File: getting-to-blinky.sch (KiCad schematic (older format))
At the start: 7 parts

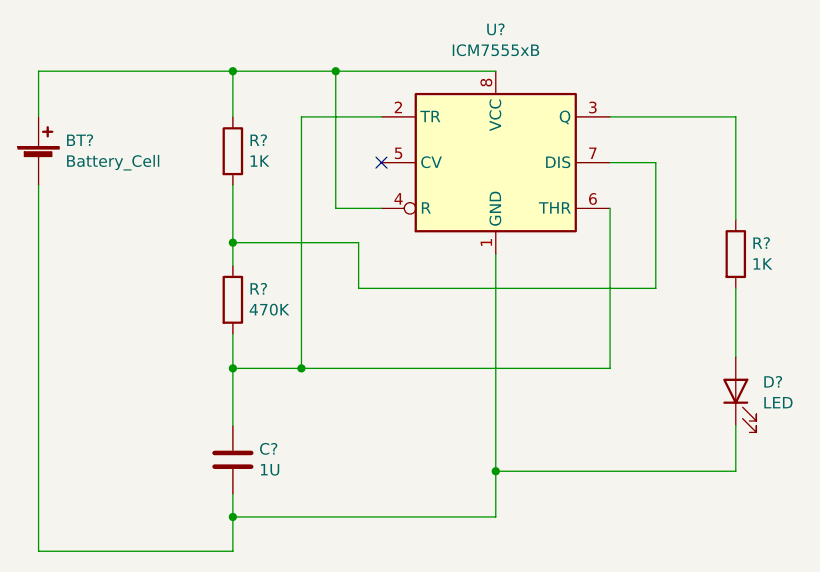
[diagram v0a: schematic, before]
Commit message: Annotate and assign footprints.
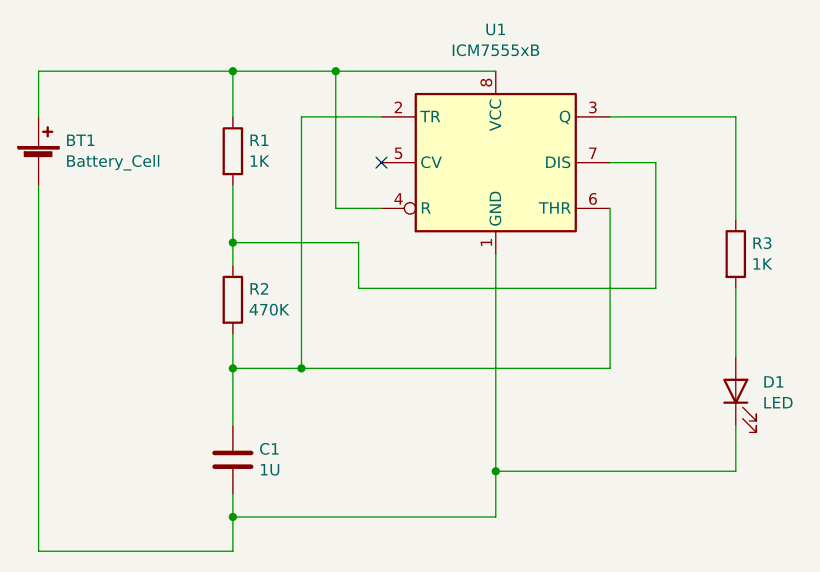
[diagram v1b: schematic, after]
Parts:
- BT1: renamed from BT?; footprint (none) -> electronics-getting-to-blinky:S8211-46R
- D1: renamed from D?; footprint (none) -> LED_SMD:LED_0805_2012Metric_Pad1.15x1.40mm_HandSolder
- gave numbers to parts that had none: 5
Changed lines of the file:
@@
 $EndDescr
 $Comp
-L Timer:ICM7555xB U?
+L Timer:ICM7555xB U1
 U 1 1 5F0270B9
 P 5550 4000
-F 0 "U?" H 5550 4581 50  0000 C CNN
+F 0 "U1" H 5550 4581 50  0000 C CNN
 F 1 "ICM7555xB" H 5550 4490 50  0000 C CNN
 F 2 "Package_SO:SOIC-8_3.9x4.9mm_P1.27mm" H 6400 3600 50  0001 C CNN
@@
 $EndComp
 $Comp
-L Device:R R?
+L Device:R R1
 U 1 1 5F0303EF
 P 4400 3950
-F 0 "R?" H 4470 3996 50  0000 L CNN
+F 0 "R1" H 4470 3996 50  0000 L CNN
 F 1 "1K" H 4470 3905 50  0000 L CNN
 F 2 "Resistor_SMD:R_0805_2012Metric_Pad1.15x1.40mm_HandSolder" V 4330 3950 50  0001 C CNN
@@
 $EndComp
 $Comp
-L Device:R R?
+L Device:R R2
 U 1 1 5F031116
 P 4400 4600
-F 0 "R?" H 4470 4646 50  0000 L CNN
+F 0 "R2" H 4470 4646 50  0000 L CNN
 F 1 "470K" H 4470 4555 50  0000 L CNN
 F 2 "Resistor_SMD:R_0805_2012Metric_Pad1.15x1.40mm_HandSolder" V 4330 4600 50  0001 C CNN
@@
 $EndComp
 $Comp
-L Device:R R?
+L Device:R R3
 U 1 1 5F031486
 P 6600 4400
-F 0 "R?" H 6670 4446 50  0000 L CNN
+F 0 "R3" H 6670 4446 50  0000 L CNN
 F 1 "1K" H 6670 4355 50  0000 L CNN
 F 2 "Resistor_SMD:R_0805_2012Metric_Pad1.15x1.40mm_HandSolder" V 6530 4400 50  0001 C CNN
@@
 $EndComp
 $Comp
-L Device:C C?
+L Device:C C1
 U 1 1 5F031D64
 P 4400 5300
-F 0 "C?" H 4515 5346 50  0000 L CNN
+F 0 "C1" H 4515 5346 50  0000 L CNN
 F 1 "1U" H 4515 5255 50  0000 L CNN
 F 2 "Capacitor_SMD:C_0805_2012Metric_Pad1.15x1.40mm_HandSolder" H 4438 5150 50  0001 C CNN
@@
 $EndComp
 $Comp
-L Device:Battery_Cell BT?
+L Device:Battery_Cell BT1
 U 1 1 5F03267C
 P 3550 4000
-F 0 "BT?" H 3668 4096 50  0000 L CNN
+F 0 "BT1" H 3668 4096 50  0000 L CNN
 F 1 "Battery_Cell" H 3668 4005 50  0000 L CNN
-F 2 "" V 3550 4060 50  0001 C CNN
+F 2 "electronics-getting-to-blinky:S8211-46R" V 3550 4060 50  0001 C CNN
 F 3 "~" V 3550 4060 50  0001 C CNN
 	1    3550 4000
@@
 $EndComp
 $Comp
-L Device:LED D?
+L Device:LED D1
 U 1 1 5F03381D
 P 6600 5000
-F 0 "D?" V 6639 4882 50  0000 R CNN
+F 0 "D1" V 6639 4882 50  0000 R CNN
 F 1 "LED" V 6548 4882 50  0000 R CNN
-F 2 "" H 6600 5000 50  0001 C CNN
+F 2 "LED_SMD:LED_0805_2012Metric_Pad1.15x1.40mm_HandSolder" H 6600 5000 50  0001 C CNN
 F 3 "~" H 6600 5000 50  0001 C CNN
 	1    6600 5000

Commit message: Add PCB layout.
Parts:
- BT1: value Battery_Cell -> CR2032
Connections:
- net GND: now reaches BT1.2 (-), C1.2, D1.1 (K), U1.1 (GND)
- net THR: now reaches C1.1, R2.2, U1.2 (TR), U1.6 (THR)
- net VDD: now reaches BT1.1 (+), R1.1, U1.4 (R), U1.8 (VCC)
- net DIS: now reaches R1.2, R2.1, U1.7 (DIS)
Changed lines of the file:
@@
 P 3550 4000
 F 0 "BT1" H 3668 4096 50  0000 L CNN
-F 1 "Battery_Cell" H 3668 4005 50  0000 L CNN
+F 1 "CR2032" H 3668 4005 50  0000 L CNN
 F 2 "electronics-getting-to-blinky:S8211-46R" V 3550 4060 50  0001 C CNN
 F 3 "~" V 3550 4060 50  0001 C CNN
@@
 	4400 5700 4400 5550
 Connection ~ 4400 5550
+Text Label 4600 3600 0    50   ~ 0
+VDD
+Text Label 4550 4900 0    50   ~ 0
+THR
+Text Label 4550 4350 0    50   ~ 0
+DIS
+Text Label 3900 5700 0    50   ~ 0
+GND
 $EndSCHEMATC
